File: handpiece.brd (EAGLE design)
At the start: 101.3 x 86.4 mm, 26 parts, among them IC1 MEGA8-P

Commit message: proof of concept routing
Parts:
- moved C1 7.62 mm to (83.8, 19.1), turned to 270 degrees
- moved A 1.27 mm to (74.9, 2.54)
- moved N4 1.27 mm to (74.9, 73.7)
- moved S 1.27 mm to (74.9, 35.6)
- moved T 1.27 mm to (74.9, 52.1)
- moved HL 1.27 mm to (58.4, 52.1)
- moved IC1 1.27 mm to (49.5, 19.1)
- moved N3 1.27 mm to (58.4, 73.7)
- moved RG 1.27 mm to (58.4, 35.6)
- moved E 1.27 mm to (8.89, 2.54)
- moved N0 1.27 mm to (8.89, 73.7)
- moved SS0 1.27 mm to (8.89, 52.1)
- moved SS1 1.27 mm to (8.89, 35.6)
- moved KR 1.27 mm to (25.4, 35.6)
- moved N1 1.27 mm to (25.4, 73.7)
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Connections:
- net D: now also IC1.15; no longer IC1.16
- net EA: now also IC1.4; no longer IC1.5
- net KR: now also IC1.2; no longer IC1.3
- net N: now also IC1.14; no longer IC1.4
- net OU: now also IC1.5; no longer IC1.6
- net SS: now also IC1.3; no longer IC1.2
- net Z: now also IC1.16; no longer IC1.15
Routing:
- net EA: track 0.00 -> 94.3 mm
- net N: track 0.00 -> 82.5 mm
- net VCC: track 0.00 -> 81.8 mm
- net SS: track 0.00 -> 76.2 mm
- net OU: track 0.00 -> 74.7 mm
- net D: track 0.00 -> 62.2 mm
- net KR: track 0.00 -> 58.4 mm
- net Z: track 0.00 -> 53.3 mm
- net T: track 0.00 -> 53.3 mm
- net HL: track 0.00 -> 49.5 mm
- net PP: track 0.00 -> 45.7 mm
- net TF: track 0.00 -> 44.5 mm
- net S: track 0.00 -> 34.3 mm
- net RG: track 0.00 -> 22.9 mm
- net WB: track 0.00 -> 21.6 mm
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- added copper zone on layer 16, net GND
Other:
- board size 101.3 x 86.4 mm -> 100 x 82.5 mm

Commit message: add second connector (only one populated on one board)
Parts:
- added CR: (no value), con-yamaichi:MDIN06SS
- renumbered X1 to CL
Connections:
- net GND: now also CR.1, CR.2
- net SCL: now also CR.6
- net SDA: now also CR.4
- net VCC: now also CR.3, CR.5
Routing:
- net VCC: track 81.8 -> 110.2 mm, vias 0 -> 2
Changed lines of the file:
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@@
 <?xml version="1.0" encoding="utf-8"?>
 <!DOCTYPE eagle SYSTEM "eagle.dtd">
-<eagle version="6.4">
+<eagle version="6.5.0">
 <drawing>
 <settings>
@@
 <setting verticaltext="up"/>
 </settings>
-<grid distance="1.27" unitdist="mm" unit="mm" style="lines" multiple="1" display="no" altdistance="0.025" altunitdist="inch" altunit="inch"/>
+<grid distance="1.27" unitdist="mm" unit="inch" style="lines" multiple="1" display="no" altdistance="0.025" altunitdist="inch" altunit="inch"/>
 <layers>
 <layer number="1" name="Top" color="4" fill="1" visible="yes" active="yes"/>
@@
 <element name="R1" library="rcl" package="0207/7" value="10k" x="27.94" y="19.05" rot="R90"/>
 <element name="C1" library="rcl" package="C075-032X103" value="100n" x="83.82" y="19.05" rot="R270"/>
-<element name="X1" library="con-yamaichi" package="MDIN06SS" value="" x="100.33" y="19.05" rot="R90">
+<element name="CL" library="con-yamaichi" package="MDIN06SS" value="" x="100.33" y="19.05" rot="R90">
 <attribute name="OC_NEWARK" value="unknown" x="100.33" y="19.05" size="1.778" layer="27" rot="R90" display="off"/>
 <attribute name="MPN" value="" x="100.33" y="19.05" size="1.778" layer="27" rot="R90" display="off"/>
 <attribute name="MF" value="" x="100.33" y="19.05" size="1.778" layer="27" rot="R90" display="off"/>
 <attribute name="OC_FARNELL" value="unknown" x="100.33" y="19.05" size="1.778" layer="27" rot="R90" display="off"/>
+</element>
+<element name="CR" library="con-yamaichi" package="MDIN06SS" value="" x="12.7" y="19.05" rot="R90">
+<attribute name="OC_NEWARK" value="unknown" x="12.7" y="19.05" size="1.778" layer="27" rot="R90" display="off"/>
+<attribute name="MPN" value="" x="12.7" y="19.05" size="1.778" layer="27" rot="R90" display="off"/>
+<attribute name="MF" value="" x="12.7" y="19.05" size="1.778" layer="27" rot="R90" display="off"/>
+<attribute name="OC_FARNELL" value="unknown" x="12.7" y="19.05" size="1.778" layer="27" rot="R90" display="off"/>
 </element>
 </elements>
@@
 <contactref element="D" pad="PIN-1"/>
 <contactref element="Z" pad="PIN-1"/>
-<contactref element="X1" pad="1"/>
-<contactref element="X1" pad="2"/>
+<contactref element="CL" pad="1"/>
+<contactref element="CL" pad="2"/>
 <contactref element="E" pad="PIN-1"/>
 <contactref element="U" pad="PIN-1"/>
@@
 <vertex x="0" y="-1.27"/>
 </polygon>
-<wire x1="54.61" y1="38.1" x2="71.12" y2="38.1" width="0" layer="19" extent="1-1"/>
+<contactref element="CR" pad="1"/>
+<contactref element="CR" pad="2"/>
+<wire x1="71.12" y1="38.1" x2="54.61" y2="38.1" width="0" layer="19" extent="1-1"/>
 </signal>
 <signal name="VCC">
@@
 <contactref element="R1" pad="2"/>
 <contactref element="C1" pad="1"/>
-<contactref element="X1" pad="3"/>
-<contactref element="X1" pad="5"/>
-<wire x1="27.94" y1="22.86" x2="27.94" y2="17.78" width="0.8128" layer="16"/>
+<contactref element="CL" pad="3"/>
+<contactref element="CL" pad="5"/>
+<wire x1="27.94" y1="22.86" x2="27.94" y2="20.32" width="0.8128" layer="16"/>
+<wire x1="27.94" y1="20.32" x2="27.94" y2="17.78" width="0.8128" layer="16"/>
 <wire x1="27.94" y1="17.78" x2="48.26" y2="17.78" width="0.8128" layer="16"/>
 <wire x1="48.26" y1="17.78" x2="48.26" y2="15.24" width="0.8128" layer="16"/>
 <wire x1="53.34" y1="22.86" x2="53.34" y2="17.78" width="0.8128" layer="16"/>
 <wire x1="53.34" y1="17.78" x2="48.26" y2="17.78" width="0.8128" layer="16"/>
-<wire x1="53.34" y1="17.78" x2="81.28" y2="17.78" width="0.8128" layer="16"/>
-<wire x1="81.28" y1="17.78" x2="81.28" y2="22.86" width="0.8128" layer="16"/>
-<wire x1="81.28" y1="22.86" x2="83.82" y2="22.86" width="0.8128" layer="16"/>
+<wire x1="53.34" y1="17.78" x2="83.82" y2="17.78" width="0.8128" layer="16"/>
+<wire x1="83.82" y1="17.78" x2="83.82" y2="22.86" width="0.8128" layer="16"/>
 <wire x1="83.82" y1="22.86" x2="88.92" y2="22.86" width="0.8128" layer="16"/>
 <wire x1="91.83" y1="22.45" x2="89.33" y2="22.45" width="0.8128" layer="16"/>
 <wire x1="89.33" y1="22.45" x2="88.92" y2="22.86" width="0.8128" layer="16"/>
+<contactref element="CR" pad="3"/>
+<contactref element="CR" pad="5"/>
+<wire x1="1.7" y1="22.45" x2="4.2" y2="22.45" width="0.8128" layer="16"/>
+<wire x1="4.2" y1="22.45" x2="13.97" y2="22.45" width="0.8128" layer="16"/>
+<wire x1="13.97" y1="22.45" x2="13.97" y2="20.32" width="0.8128" layer="16"/>
+<via x="13.97" y="20.32" extent="1-16" drill="0.6" diameter="1.778" shape="square"/>
+<wire x1="13.97" y1="20.32" x2="20.32" y2="20.32" width="0.8128" layer="1"/>
+<via x="20.32" y="20.32" extent="1-16" drill="0.6" diameter="1.778" shape="square"/>
+<wire x1="20.32" y1="20.32" x2="27.94" y2="20.32" width="0.8128" layer="16"/>
 </signal>
 <signal name="N$2">
@@
 <contactref element="IC1" pad="3"/>
 <wire x1="38.1" y1="15.24" x2="38.1" y2="11.43" width="0.8128" layer="16"/>
-<wire x1="38.1" y1="11.43" x2="11.43" y2="11.43" width="0.8128" layer="16"/>
-<wire x1="11.43" y1="11.43" x2="11.43" y2="40.64" width="0.8128" layer="16"/>
+<wire x1="38.1" y1="11.43" x2="16.51" y2="11.43" width="0.8128" layer="16"/>
+<wire x1="16.51" y1="11.43" x2="16.51" y2="26.67" width="0.8128" layer="16"/>
+<wire x1="16.51" y1="26.67" x2="11.43" y2="26.67" width="0.8128" layer="16"/>
+<wire x1="11.43" y1="26.67" x2="11.43" y2="40.64" width="0.8128" layer="16"/>
 </signal>
 <signal name="TF">
@@
 <signal name="SCL">
 <contactref element="IC1" pad="28"/>
-<contactref element="X1" pad="6"/>
+<contactref element="CL" pad="6"/>
+<contactref element="CR" pad="6"/>
 <wire x1="33.02" y1="22.86" x2="89.33" y2="15.65" width="0" layer="19" extent="1-1"/>
+<wire x1="1.7" y1="15.65" x2="33.02" y2="22.86" width="0" layer="19" extent="1-1"/>
 </signal>
 <signal name="SDA">
 <contactref element="IC1" pad="27"/>
-<contactref element="X1" pad="4"/>
+<contactref element="CL" pad="4"/>
+<contactref element="CR" pad="4"/>
 <wire x1="35.56" y1="22.86" x2="91.83" y2="15.65" width="0" layer="19" extent="1-1"/>
+<wire x1="4.2" y1="15.65" x2="35.56" y2="22.86" width="0" layer="19" extent="1-1"/>
 </signal>
 </signals>

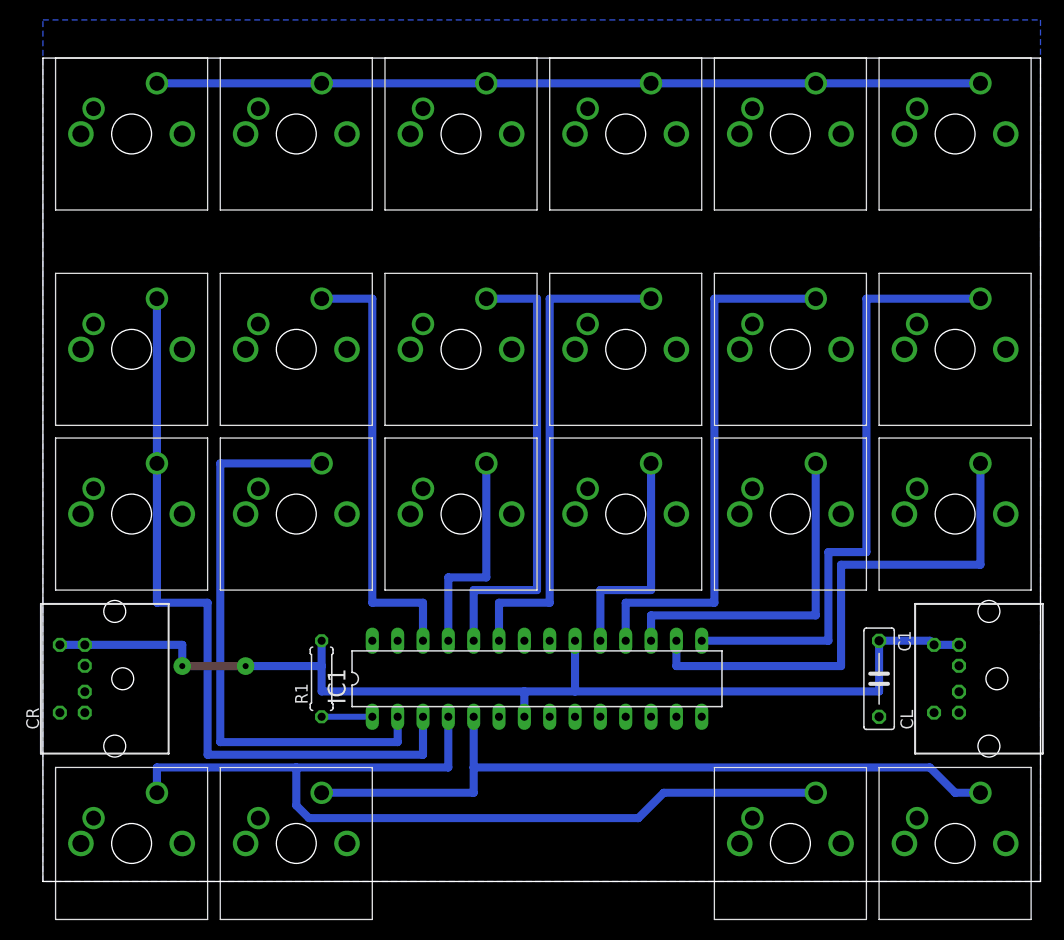
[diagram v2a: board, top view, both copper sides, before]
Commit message: wire i²c
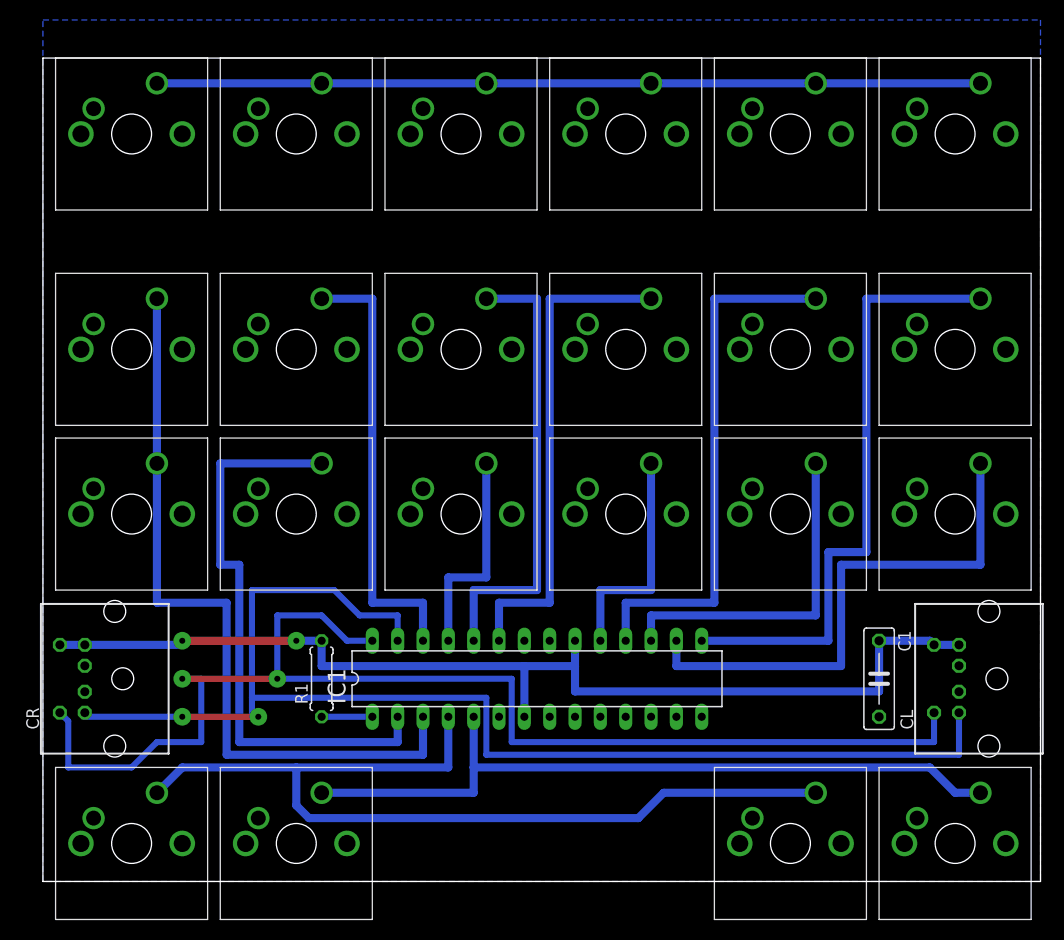
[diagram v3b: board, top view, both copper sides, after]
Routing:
- net SDA: track 0.00 -> 130.1 mm, vias 0 -> 2
- net SCL: track 0.00 -> 130.1 mm, vias 0 -> 2
- net VCC: track 110.2 -> 108.5 mm
- net EA: track 94.3 -> 92.8 mm
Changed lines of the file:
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@@
 <setting verticaltext="up"/>
 </settings>
-<grid distance="1.27" unitdist="mm" unit="inch" style="lines" multiple="1" display="no" altdistance="0.025" altunitdist="inch" altunit="inch"/>
+<grid distance="0.05" unitdist="inch" unit="inch" style="lines" multiple="1" display="yes" altdistance="0.025" altunitdist="inch" altunit="inch"/>
 <layers>
 <layer number="1" name="Top" color="4" fill="1" visible="yes" active="yes"/>
@@
 <contactref element="A" pad="PIN-1"/>
 <contactref element="O" pad="PIN-1"/>
-<polygon width="0.4064" layer="16" isolate="0.4064">
+<polygon width="0.4064" layer="16" isolate="0.4064" orphans="yes">
 <vertex x="0" y="85.09"/>
 <vertex x="100" y="85.09"/>
@@
 <contactref element="CR" pad="1"/>
 <contactref element="CR" pad="2"/>
+<wire x1="50.8" y1="15.24" x2="50.8" y2="22.86" width="0" layer="19" extent="1-1"/>
 <wire x1="71.12" y1="38.1" x2="54.61" y2="38.1" width="0" layer="19" extent="1-1"/>
 </signal>
@@
 <contactref element="CL" pad="5"/>
 <wire x1="27.94" y1="22.86" x2="27.94" y2="20.32" width="0.8128" layer="16"/>
-<wire x1="27.94" y1="20.32" x2="27.94" y2="17.78" width="0.8128" layer="16"/>
-<wire x1="27.94" y1="17.78" x2="48.26" y2="17.78" width="0.8128" layer="16"/>
-<wire x1="48.26" y1="17.78" x2="48.26" y2="15.24" width="0.8128" layer="16"/>
-<wire x1="53.34" y1="22.86" x2="53.34" y2="17.78" width="0.8128" layer="16"/>
-<wire x1="53.34" y1="17.78" x2="48.26" y2="17.78" width="0.8128" layer="16"/>
+<wire x1="27.94" y1="20.32" x2="48.26" y2="20.32" width="0.8128" layer="16"/>
+<wire x1="48.26" y1="20.32" x2="48.26" y2="15.24" width="0.8128" layer="16"/>
+<wire x1="53.34" y1="22.86" x2="53.34" y2="20.32" width="0.8128" layer="16"/>
 <wire x1="53.34" y1="17.78" x2="83.82" y2="17.78" width="0.8128" layer="16"/>
 <wire x1="83.82" y1="17.78" x2="83.82" y2="22.86" width="0.8128" layer="16"/>
@@
 <wire x1="1.7" y1="22.45" x2="4.2" y2="22.45" width="0.8128" layer="16"/>
 <wire x1="4.2" y1="22.45" x2="13.97" y2="22.45" width="0.8128" layer="16"/>
-<wire x1="13.97" y1="22.45" x2="13.97" y2="20.32" width="0.8128" layer="16"/>
-<via x="13.97" y="20.32" extent="1-16" drill="0.6" diameter="1.778" shape="square"/>
-<wire x1="13.97" y1="20.32" x2="20.32" y2="20.32" width="0.8128" layer="1"/>
-<via x="20.32" y="20.32" extent="1-16" drill="0.6" diameter="1.778" shape="square"/>
-<wire x1="20.32" y1="20.32" x2="27.94" y2="20.32" width="0.8128" layer="16"/>
+<wire x1="13.97" y1="22.45" x2="13.97" y2="22.86" width="0.8128" layer="16"/>
+<via x="13.97" y="22.86" extent="1-16" drill="0.6" diameter="1.778" shape="square"/>
+<wire x1="13.97" y1="22.86" x2="25.4" y2="22.86" width="0.8128" layer="1"/>
+<via x="25.4" y="22.86" extent="1-16" drill="0.6" diameter="1.778" shape="square"/>
+<wire x1="53.34" y1="17.78" x2="53.34" y2="20.32" width="0.8128" layer="16"/>
+<wire x1="53.34" y1="20.32" x2="48.26" y2="20.32" width="0.8128" layer="16"/>
+<wire x1="25.4" y1="22.86" x2="27.94" y2="22.86" width="0.8128" layer="16"/>
 </signal>
 <signal name="N$2">
@@
 <contactref element="IC1" pad="3"/>
 <wire x1="38.1" y1="15.24" x2="38.1" y2="11.43" width="0.8128" layer="16"/>
-<wire x1="38.1" y1="11.43" x2="16.51" y2="11.43" width="0.8128" layer="16"/>
-<wire x1="16.51" y1="11.43" x2="16.51" y2="26.67" width="0.8128" layer="16"/>
-<wire x1="16.51" y1="26.67" x2="11.43" y2="26.67" width="0.8128" layer="16"/>
+<wire x1="38.1" y1="11.43" x2="18.415" y2="11.43" width="0.8128" layer="16"/>
+<wire x1="18.415" y1="11.43" x2="18.415" y2="26.67" width="0.8128" layer="16"/>
+<wire x1="18.415" y1="26.67" x2="11.43" y2="26.67" width="0.8128" layer="16"/>
 <wire x1="11.43" y1="26.67" x2="11.43" y2="40.64" width="0.8128" layer="16"/>
 </signal>
@@
 <contactref element="IC1" pad="2"/>
 <wire x1="27.94" y1="40.64" x2="17.78" y2="40.64" width="0.8128" layer="16"/>
-<wire x1="17.78" y1="40.64" x2="17.78" y2="12.7" width="0.8128" layer="16"/>
-<wire x1="17.78" y1="12.7" x2="35.56" y2="12.7" width="0.8128" layer="16"/>
+<wire x1="17.78" y1="40.64" x2="17.78" y2="30.48" width="0.8128" layer="16"/>
+<wire x1="17.78" y1="30.48" x2="19.685" y2="30.48" width="0.8128" layer="16"/>
+<wire x1="19.685" y1="30.48" x2="19.685" y2="12.7" width="0.8128" layer="16"/>
+<wire x1="19.685" y1="12.7" x2="35.56" y2="12.7" width="0.8128" layer="16"/>
 <wire x1="35.56" y1="12.7" x2="35.56" y2="15.24" width="0.8128" layer="16"/>
 </signal>
@@
 <signal name="EA">
 <contactref element="E" pad="PIN-2"/>
-<wire x1="11.43" y1="7.62" x2="11.43" y2="10.16" width="0.8128" layer="16"/>
-<wire x1="11.43" y1="10.16" x2="25.4" y2="10.16" width="0.8128" layer="16"/>
+<wire x1="11.43" y1="7.62" x2="13.97" y2="10.16" width="0.8128" layer="16"/>
+<wire x1="13.97" y1="10.16" x2="25.4" y2="10.16" width="0.8128" layer="16"/>
 <wire x1="25.4" y1="10.16" x2="40.64" y2="10.16" width="0.8128" layer="16"/>
 <contactref element="A" pad="PIN-2"/>
@@
 <contactref element="CL" pad="6"/>
 <contactref element="CR" pad="6"/>
-<wire x1="33.02" y1="22.86" x2="89.33" y2="15.65" width="0" layer="19" extent="1-1"/>
-<wire x1="1.7" y1="15.65" x2="33.02" y2="22.86" width="0" layer="19" extent="1-1"/>
+<wire x1="89.33" y1="15.65" x2="89.33" y2="12.7" width="0.6096" layer="16"/>
+<wire x1="89.33" y1="12.7" x2="46.99" y2="12.7" width="0.6096" layer="16"/>
+<wire x1="46.99" y1="12.7" x2="46.99" y2="19.05" width="0.6096" layer="16"/>
+<wire x1="46.99" y1="19.05" x2="23.495" y2="19.05" width="0.6096" layer="16"/>
+<wire x1="23.495" y1="19.05" x2="23.495" y2="25.4" width="0.6096" layer="16"/>
+<wire x1="23.495" y1="25.4" x2="27.94" y2="25.4" width="0.6096" layer="16"/>
+<wire x1="27.94" y1="25.4" x2="30.48" y2="22.86" width="0.6096" layer="16"/>
+<wire x1="30.48" y1="22.86" x2="33.02" y2="22.86" width="0.6096" layer="16"/>
+<wire x1="23.495" y1="19.05" x2="13.97" y2="19.05" width="0.6096" layer="1"/>
+<wire x1="13.97" y1="19.05" x2="15.875" y2="19.05" width="0.6096" layer="16"/>
+<wire x1="15.875" y1="19.05" x2="15.875" y2="12.7" width="0.6096" layer="16"/>
+<wire x1="15.875" y1="12.7" x2="11.43" y2="12.7" width="0.6096" layer="16"/>
+<wire x1="11.43" y1="12.7" x2="8.89" y2="10.16" width="0.6096" layer="16"/>
+<wire x1="8.89" y1="10.16" x2="2.54" y2="10.16" width="0.6096" layer="16"/>
+<wire x1="2.54" y1="10.16" x2="2.54" y2="14.81" width="0.6096" layer="16"/>
+<wire x1="2.54" y1="14.81" x2="1.7" y2="15.65" width="0.6096" layer="16"/>
+<via x="13.97" y="19.05" extent="1-16" drill="0.6" diameter="1.778" shape="square"/>
+<via x="23.495" y="19.05" extent="1-16" drill="0.6" diameter="1.778" shape="square"/>
 </signal>
 <signal name="SDA">
@@
 <contactref element="CL" pad="4"/>
 <contactref element="CR" pad="4"/>
-<wire x1="35.56" y1="22.86" x2="91.83" y2="15.65" width="0" layer="19" extent="1-1"/>
-<wire x1="4.2" y1="15.65" x2="35.56" y2="22.86" width="0" layer="19" extent="1-1"/>
+<wire x1="91.83" y1="15.65" x2="91.83" y2="11.43" width="0.6096" layer="16"/>
+<wire x1="91.83" y1="11.43" x2="44.45" y2="11.43" width="0.6096" layer="16"/>
+<wire x1="44.45" y1="11.43" x2="44.45" y2="17.145" width="0.6096" layer="16"/>
+<wire x1="44.45" y1="17.145" x2="20.955" y2="17.145" width="0.6096" layer="16"/>
+<wire x1="35.56" y1="22.86" x2="35.56" y2="25.4" width="0.6096" layer="16"/>
+<wire x1="35.56" y1="25.4" x2="31.75" y2="25.4" width="0.6096" layer="16"/>
+<wire x1="31.75" y1="25.4" x2="29.21" y2="27.94" width="0.6096" layer="16"/>
+<wire x1="29.21" y1="27.94" x2="20.955" y2="27.94" width="0.6096" layer="16"/>
+<wire x1="20.955" y1="27.94" x2="20.955" y2="17.145" width="0.6096" layer="16"/>
+<wire x1="20.955" y1="17.145" x2="20.955" y2="15.24" width="0.6096" layer="16"/>
+<wire x1="20.955" y1="15.24" x2="21.59" y2="15.24" width="0.6096" layer="16"/>
+<wire x1="21.59" y1="15.24" x2="13.97" y2="15.24" width="0.6096" layer="1"/>
+<wire x1="13.97" y1="15.24" x2="4.2" y2="15.24" width="0.6096" layer="16"/>
+<wire x1="4.2" y1="15.24" x2="4.2" y2="15.65" width="0.6096" layer="16"/>
+<via x="13.97" y="15.24" extent="1-16" drill="0.6" diameter="1.778" shape="square"/>
+<via x="21.59" y="15.24" extent="1-16" drill="0.6" diameter="1.778" shape="square"/>
 </signal>
 </signals>
